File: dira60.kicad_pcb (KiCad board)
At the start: 2 copper layers, 199 parts, among them J0 USB_C_Receptacle, SW0 RESET, U0 ATmega32U4-AU, X0 XTAL_GND

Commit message: Added type C
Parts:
- removed R0: 10k, Resistor_SMD:R_0805_2012Metric_Pad1.15x1.40mm_HandSolder
- removed the REF** at (271.5, 28.5)
- removed SW0: RESET, random-keyboard-parts:SKQG-1155865
- added C11: 4.7u, Capacitor_SMD:C_0805_2012Metric_Pad1.15x1.40mm_HandSolder, F.Cu at (32.8, 152.5)
- added D60: D_Small, Diode_SMD:D_SOD-123, B.Cu at (251.0, 105.2)
- added MX60: MX-1U, keyboard_parts:Kailh_MX_Socket_LED, B.Cu at (247.8, 104.5)
- added REF**: 1U, MX_Alps_Hybrid:MX-1U, F.Cu at (262.0, 28.5)
- added REF**: 1U, MX_Alps_Hybrid:MX-1U, F.Cu at (281.0, 28.5)
- added USB0: HRO-TYPE-C-31-M-12, Type-C:HRO-TYPE-C-31-M-12-HandSoldering, F.Cu at (25.0, 165.7)
- D2: value D -> D_Small
- J0: footprint Type-C:HRO-TYPE-C-31-M-12-HandSoldering -> Connector_USB:USB3_A_Molex_48393-001
- MX14, MX41: value MX-2U -> MX-1U
- MX15, MX28, MX56: value MX-1.5U -> MX-1U
- MX16, MX59: value MX-1U -> MX-1.5U
- MX29: value MX-1.75U -> MX-1.5U
- MX30, MX54: value MX-1U -> MX-1.75U
- MX42: value MX-2.25U -> MX-2U
- MX43: value MX-1U -> MX-2.25U
- MX53: value MX-1.75U -> MX-1U
- MX57: value MX-7U -> MX-1.5U
- MX58: value MX-1.5U -> MX-7U
- R4: moved to F.Cu
- U0: footprint Package_QFP:TQFP-44_10x10mm_P0.8mm -> keyboard_parts:QFN-44-1EP_7x7mm_Pitch0.5mm
- moved MX15 261.9 mm to (281.0, 28.5)
- moved D16 257.8 mm to (23.0, 48.2)
- moved MX29 254.8 mm to (276.3, 47.5)
- moved D30 254.0 mm to (25.3, 67.2)
- moved D43 247.3 mm to (30.1, 86.3)
- moved MX42 243.0 mm to (269.2, 66.5)
- moved D17 241.7 mm to (46.7, 48.2)
- moved MX55 238.3 mm to (281.0, 85.5)
- moved D56 232.9 mm to (46.7, 105.2)
- moved D31 231.7 mm to (51.5, 67.2)
- moved C3 226.5 mm to (31.8, 63.3), turned to 90 degrees
- moved D44 220.8 mm to (61.0, 86.2)
- moved C9 219.7 mm to (39.8, 58.8), turned to 90 degrees
- moved R2 219.2 mm to (16.5, 150.3)
- moved C10 215.7 mm to (31.8, 58.8), turned to 90 degrees
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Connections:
- C8 pad 1: GND -> Net-(C8-Pad1)
- C8 pad 2: Net-(C8-Pad2) -> GND
- D15 pad 1: ROW1 -> ROW0
- D29 pad 1: ROW2 -> ROW1
- D42 pad 1: ROW3 -> ROW2
- D55 pad 1: ROW4 -> ROW3
- MX15 pad 1: COL0 -> COL14
- MX16 pad 1: COL2 -> COL0
- MX17 pad 1: COL3 -> COL2
- MX18 pad 1: COL4 -> COL3
- MX19 pad 1: COL5 -> COL4
- MX20 pad 1: COL6 -> COL5
- MX21 pad 1: COL7 -> COL6
- MX22 pad 1: COL8 -> COL7
- MX23 pad 1: COL9 -> COL8
- MX24 pad 1: COL10 -> COL9
- MX25 pad 1: COL11 -> COL10
- MX26 pad 1: COL12 -> COL11
- MX27 pad 1: Net-(MX27-Pad1) -> COL12
- MX29 pad 1: COL0 -> COL14
- MX30 pad 1: COL2 -> COL0
- MX31 pad 1: COL3 -> COL2
- MX32 pad 1: COL4 -> COL3
- MX33 pad 1: COL5 -> COL4
- MX34 pad 1: COL6 -> COL5
- MX35 pad 1: COL7 -> COL6
- MX36 pad 1: COL8 -> COL7
- MX37 pad 1: COL9 -> COL8
- MX38 pad 1: COL10 -> COL9
- MX39 pad 1: COL11 -> COL10
- MX40 pad 1: COL12 -> COL11
- MX41 pad 1: Net-(MX27-Pad1) -> COL12
- MX42 pad 1: COL1 -> COL13
- MX43 pad 1: COL2 -> COL1
- MX44 pad 1: COL3 -> COL2
- MX45 pad 1: COL4 -> COL3
- MX46 pad 1: COL5 -> COL4
- MX47 pad 1: COL6 -> COL5
- MX48 pad 1: COL7 -> COL6
- MX49 pad 1: COL8 -> COL7
- MX50 pad 1: COL9 -> COL8
- MX51 pad 1: COL10 -> COL9
- MX52 pad 1: COL11 -> COL10
- MX53 pad 1: Net-(MX27-Pad1) -> COL11
- MX55 pad 1: COL2 -> COL14
- MX56 pad 1: COL3 -> COL2
- MX57 pad 1: Net-(MX57-Pad1) -> COL3
- MX58 pad 1: COL11 -> Net-(MX58-Pad1)
- MX59 pad 1: Net-(MX27-Pad1) -> COL11
- R4 pad 1: GND -> Net-(C8-Pad1)
- R4 pad 2: Net-(C8-Pad2) -> GND
- U0 pad 13: RESET -> Net-(U0-Pad13)
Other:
- board outline added: 285 x 95 mm

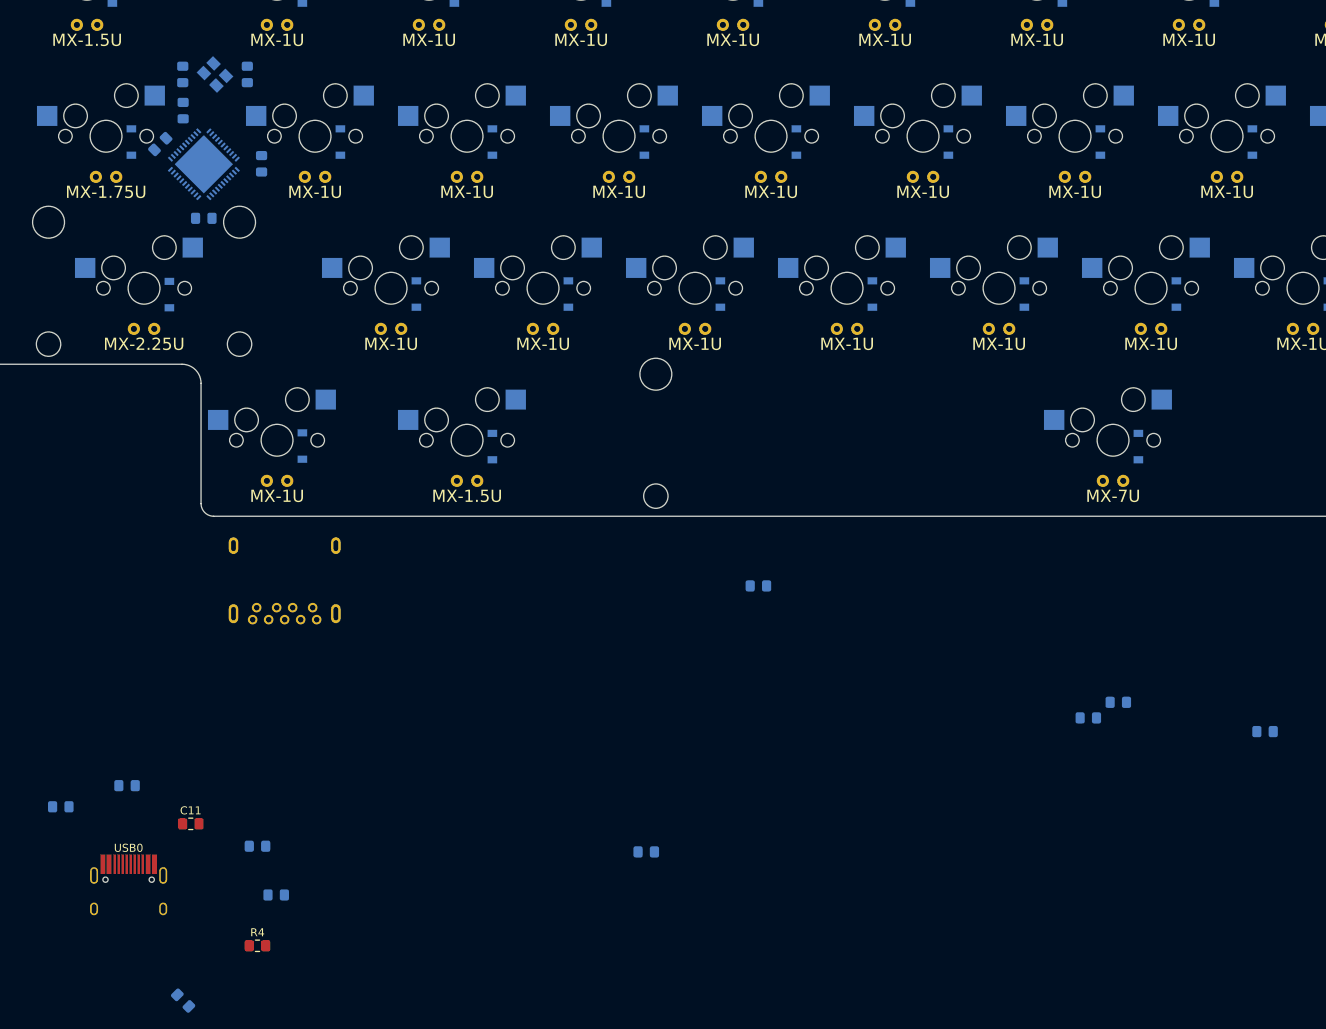
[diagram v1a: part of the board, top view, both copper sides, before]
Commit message: Placed Microcontroller
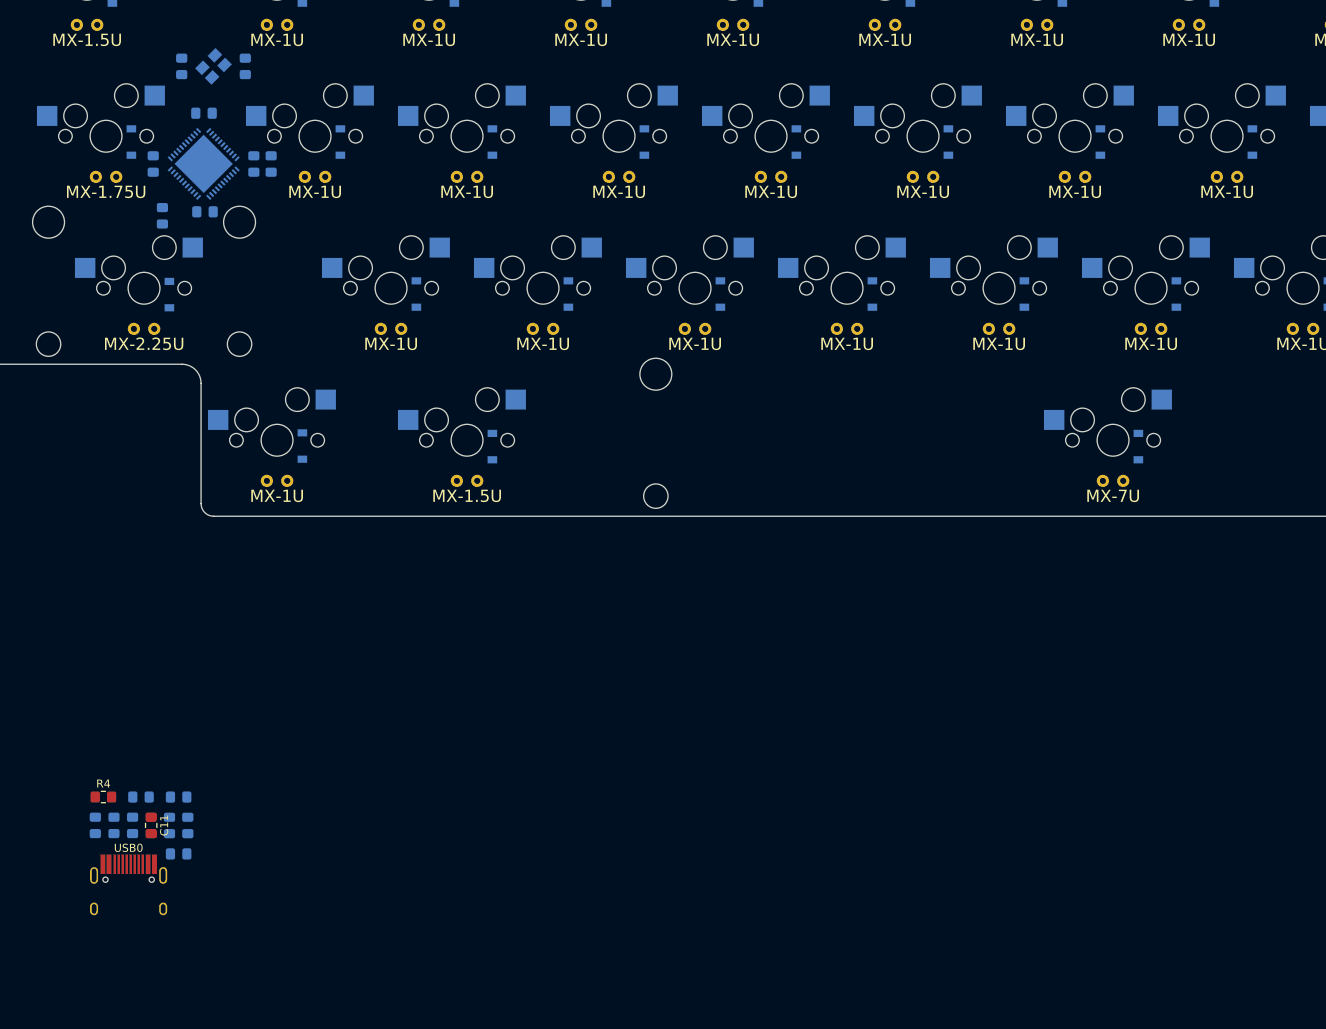
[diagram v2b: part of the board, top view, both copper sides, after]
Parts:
- removed J0: USB_C_Receptacle, Connector_USB:USB3_A_Molex_48393-001
- moved C8 136.7 mm to (31.2, 156.2)
- moved R1 118.1 mm to (31.2, 149.1), turned to 180 degrees
- moved C7 113.4 mm to (32.4, 152.7), turned to 270 degrees
- moved C1 97.9 mm to (42.8, 70.0), turned to 270 degrees
- moved C2 87.7 mm to (29.2, 76.4), turned to 90 degrees
- moved R4 26.8 mm to (21.8, 149.1)
- moved R5 22.0 mm to (30.1, 152.7), turned to 270 degrees
- moved R3 19.9 mm to (25.5, 152.6), turned to 270 degrees
- moved R6 18.1 mm to (23.2, 152.6), turned to 90 degrees
- moved C11 4.95 mm to (27.8, 152.6), turned to 270 degrees
- moved R2 4.91 mm to (20.8, 152.6), turned to 270 degrees
- moved C4 2.64 mm to (28.1, 70.0), turned to 270 degrees
- moved C3 2.63 mm to (34.4, 63.6), turned to 180 degrees
- moved C0 2.25 mm to (26.5, 149.1)
- moved C9 1.04 mm to (39.6, 57.8)
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
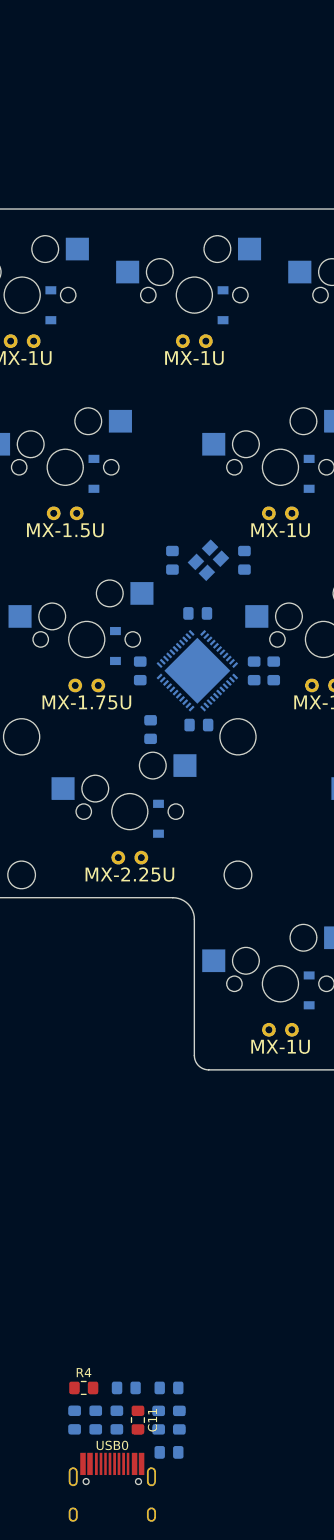
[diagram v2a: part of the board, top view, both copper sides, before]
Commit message: Routed CPU's parts
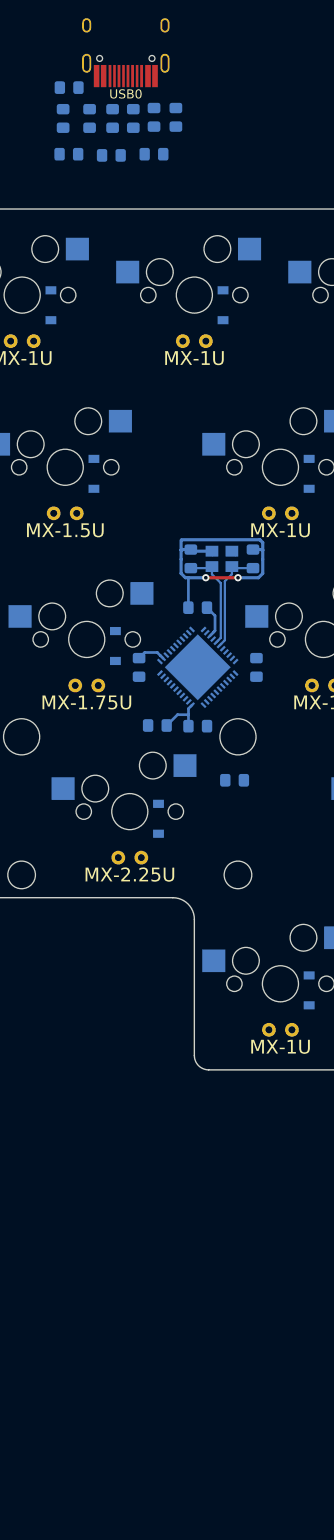
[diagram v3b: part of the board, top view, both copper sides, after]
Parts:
- C11, R4: moved to B.Cu
- moved USB0 169.6 mm to (26.5, -3.87), turned to 180 degrees
- moved C8 151.0 mm to (20.2, 5.61), turned to 180 degrees
- moved R2 144.2 mm to (32.0, 8.88), turned to 90 degrees
- moved R5 144.0 mm to (19.6, 9.01), turned to 90 degrees
- moved C7 144.0 mm to (22.5, 9.01), turned to 90 degrees
- moved R6 143.9 mm to (29.6, 8.88)
- moved C11 143.7 mm to (25.0, 9.01)
- moved R3 143.6 mm to (27.3, 9.01), turned to 90 degrees
- moved R1 136.6 mm to (20.2, 13.0)
- moved C0 136.2 mm to (29.6, 13.0), turned to 180 degrees
- moved R4 136.1 mm to (24.9, 13.1), turned to 180 degrees
- moved C1 12.8 mm to (38.5, 82.0), turned to 0 degrees
- moved C10 2.04 mm to (33.7, 57.6)
- moved X0 1.49 mm to (37.1, 57.6), turned to 180 degrees
- moved C9 0.95 mm to (40.5, 57.6)
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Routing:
- net GND: track 0.00 -> 33.5 mm, vias 0 -> 2
- net VCC: track 0.00 -> 12.3 mm
- net XTAL1: track 0.00 -> 11.4 mm
- net XTAL2: track 0.00 -> 11.1 mm
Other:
- net class Power added: clearance 0.2, trace_width 0.3, via_dia 0.8, via_drill 0.4

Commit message: Added col 7-14
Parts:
- X0: footprint Crystal:Crystal_SMD_3225-4Pin_3.2x2.5mm -> keyboard_parts:FA-238
- moved C10 0.77 mm to (32.9, 57.5)
- moved C3 0.70 mm to (34.4, 62.3), turned to 135 degrees
- moved C9 0.38 mm to (40.6, 58.0)
- moved X0 0.33 mm to (36.8, 57.7), turned to 225 degrees
- moved C6 0.31 mm to (41.0, 69.3)
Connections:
- C9 pad 1: XTAL1 -> GND
- C9 pad 2: GND -> XTAL1
- U0 pad 25: Net-(U0-Pad25) -> COL12
- U0 pad 26: Net-(U0-Pad26) -> COL14
- U0 pad 27: Net-(U0-Pad27) -> COL13
- U0 pad 28: Net-(U0-Pad28) -> COL11
- U0 pad 29: Net-(U0-Pad29) -> COL10
- U0 pad 30: Net-(U0-Pad30) -> COL9
- U0 pad 31: Net-(U0-Pad31) -> COL8
- U0 pad 32: Net-(U0-Pad32) -> COL7
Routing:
- net COL12: track 0.00 -> 318.4 mm
- net ROW0: track 0.00 -> 266.0 mm
- net ROW2: track 0.00 -> 258.6 mm, vias 0 -> 2
- net ROW1: track 0.00 -> 256.5 mm
- net ROW3: track 0.00 -> 254.2 mm
- net COL14: track 0.00 -> 247.1 mm
- net COL13: track 0.00 -> 217.9 mm
- net ROW4: track 0.00 -> 204.3 mm
- net COL11: track 0.00 -> 192.1 mm
- net COL10: track 0.00 -> 173.2 mm
- net COL9: track 0.00 -> 154.4 mm
- net COL8: track 0.00 -> 135.3 mm
- net COL7: track 0.00 -> 116.6 mm
- net Net-(D42-Pad2): track 0.00 -> 5.93 mm
- net Net-(D58-Pad2): track 0.00 -> 5.93 mm
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
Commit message: Routed all cols
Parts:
- moved D30 8.87 mm to (17.1, 70.5)
- moved C10 0.89 mm to (32.0, 57.5)
- moved C5 0.89 mm to (33.5, 76.1)
- moved C6 0.89 mm to (40.1, 69.3)
- moved C9 0.89 mm to (39.8, 58.0)
- moved U0 0.89 mm to (33.5, 69.6)
- moved X0 0.89 mm to (35.9, 57.7)
- moved C2 0.89 mm to (29.1, 76.0)
- moved C3 0.89 mm to (33.5, 62.3)
- moved C4 0.51 mm to (27.4, 69.7), turned to 90 degrees
- turned C1 to 180 degrees
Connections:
- U0 pad 18: Net-(U0-Pad18) -> COL6
- U0 pad 19: Net-(U0-Pad19) -> COL5
- U0 pad 20: Net-(U0-Pad20) -> COL4
- U0 pad 21: Net-(U0-Pad21) -> COL3
- U0 pad 22: Net-(U0-Pad22) -> COL2
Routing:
- net COL6: track 0.00 -> 177.8 mm, vias 0 -> 5
- net COL5: track 0.00 -> 160.7 mm, vias 0 -> 5
- net COL3: track 0.00 -> 147.3 mm, vias 0 -> 6
- net COL4: track 0.00 -> 140.2 mm, vias 0 -> 5
- net COL2: track 0.00 -> 130.3 mm, vias 0 -> 6
- net COL13: track 217.9 -> 338.1 mm, vias 0 -> 6
- net COL10: track 173.2 -> 260.1 mm, vias 0 -> 5
- net COL11: track 192.1 -> 278.8 mm, vias 0 -> 5
- net COL7: track 116.6 -> 202.7 mm, vias 0 -> 5
- net COL8: track 135.3 -> 221.4 mm, vias 0 -> 5
- net COL9: track 154.4 -> 240.0 mm, vias 0 -> 5
- net COL14: track 247.1 -> 330.4 mm, vias 0 -> 4
- net COL1: track 0.00 -> 75.4 mm, vias 0 -> 2
- net COL12: track 318.4 -> 377.5 mm, vias 0 -> 4
- net COL0: track 0.00 -> 44.2 mm, vias 0 -> 4
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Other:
- board size 285 x 95 mm -> 285 x 94.5 mm

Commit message: Routed all cols
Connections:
- MX58 pad 1: Net-(MX58-Pad1) -> COL7
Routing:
- net COL7: track 202.7 -> 229.6 mm, vias 5 -> 6
- net COL1: track 75.4 -> 85.4 mm
- net COL0: track 44.2 -> 41.5 mm, vias 4 -> 2

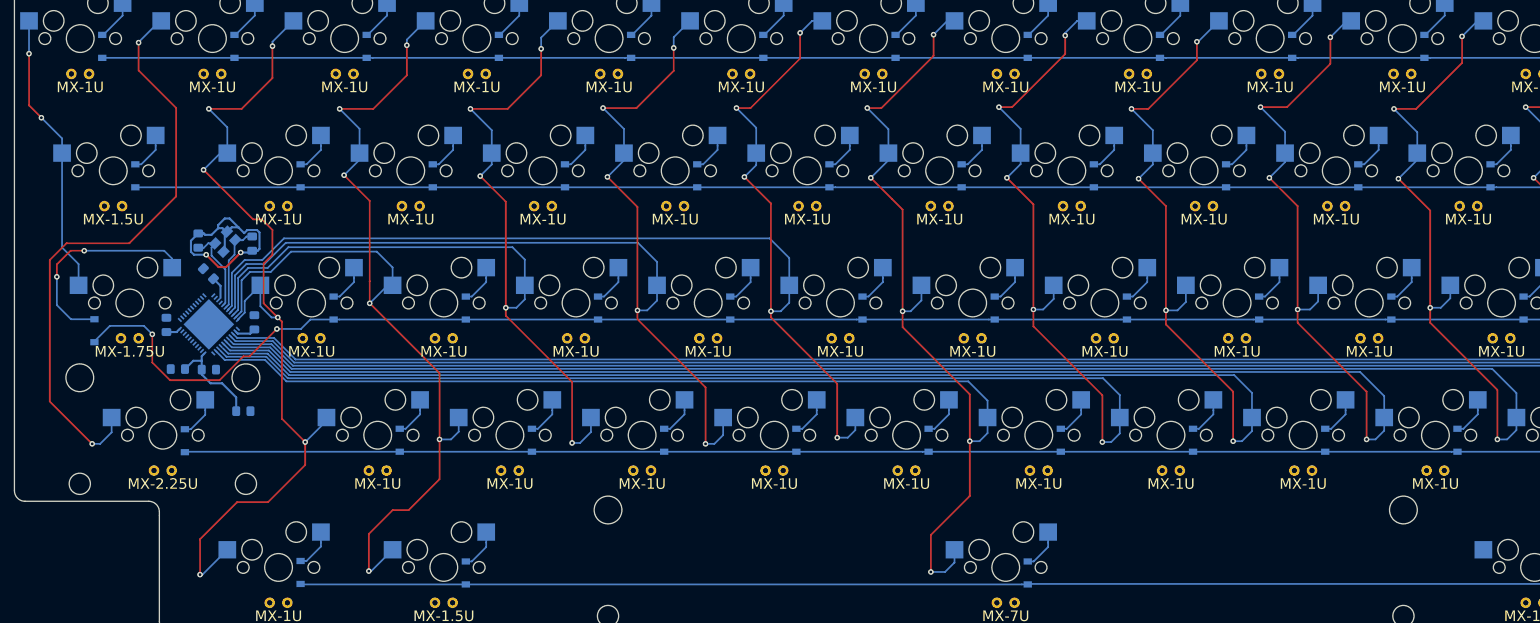
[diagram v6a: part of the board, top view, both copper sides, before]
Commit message: Routed all rows & columns
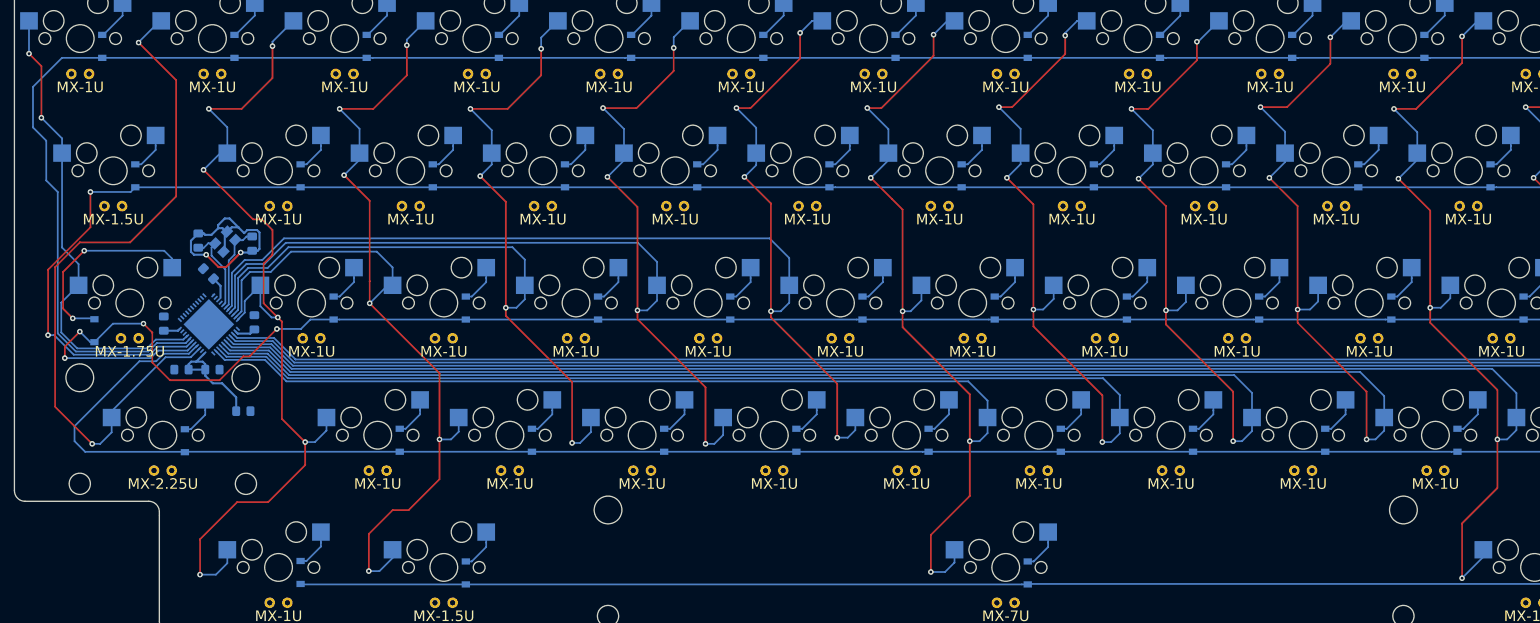
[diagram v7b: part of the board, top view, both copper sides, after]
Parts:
- moved C2 0.52 mm to (29.6, 76.1)
- moved C5 0.51 mm to (34.0, 76.1)
- moved C4 0.43 mm to (27.1, 69.5)
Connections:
- U0 pad 12: Net-(U0-Pad12) -> ROW4
- U0 pad 36: Net-(U0-Pad36) -> COL1
- U0 pad 37: Net-(U0-Pad37) -> ROW3
- U0 pad 38: Net-(U0-Pad38) -> ROW2
- U0 pad 39: Net-(U0-Pad39) -> ROW1
- U0 pad 40: Net-(U0-Pad40) -> ROW0
- U0 pad 41: Net-(U0-Pad41) -> COL0
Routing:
- net ROW0: track 266.0 -> 335.4 mm
- net ROW1: track 256.5 -> 309.0 mm, vias 0 -> 2
- net ROW3: track 254.2 -> 295.2 mm
- net COL0: track 41.5 -> 69.1 mm
- net ROW2: track 265.7 -> 293.1 mm, vias 2 -> 4
- net COL11: track 278.8 -> 306.2 mm, vias 5 -> 6
- net COL1: track 85.4 -> 101.0 mm
- net VCC: track 22.8 -> 25.7 mm
- net Net-(D30-Pad2): track 31.3 -> 29.1 mm
- net COL2: track 130.3 -> 132.2 mm
- net COL3: track 147.3 -> 148.0 mm
